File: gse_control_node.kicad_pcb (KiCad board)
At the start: 4 copper layers, 111.5 x 77 mm, 130 parts, among them J1 Conn_01x04, J10 Conn_01x04, J2 Conn_01x02, J3 Conn_02x01, J4 Conn_01x02, J5 Conn_01x02, J6 Conn_01x02, J7 Conn_02x04_Counter_Clockwise, J8 Conn_02x04_Counter_Clockwise, J9 Conn_01x04, Q3 BSS138, Q4 BSS138, Q5 BSS138, U1 ESP32-S2-DevKitC-1, U2 LM3880-1AA, U3 LMR33630BDDA, U4 LMR33630BDDA, U5 TPS78533QKVURQ1, U6 TPS78450QDBVRQ1, U7 ADS112C04, U8 ADS112C04, U9 ADS112C04

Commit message: do some pcb routing
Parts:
- removed C34, C35, C38, C39, C40, C41: 150nF, Capacitor_SMD:C_0402_1005Metric
- removed C36, C37: 0.1μF, Capacitor_SMD:C_0402_1005Metric
- removed D15, D16, D17: BAT54SW, Package_TO_SOT_SMD:SOT-323_SC-70
- removed D18, D19, D20: SK44BL, Diode_SMD:D_SMB
- removed R32, R33, R34: 1k, Resistor_SMD:R_0402_1005Metric
- removed R35: 10k, Resistor_SMD:R_0402_1005Metric
- removed R36, R38, R40: 100, Resistor_SMD:R_0402_1005Metric
- removed R37, R39, R41: 100k, Resistor_SMD:R_0603_1608Metric
- removed U7, U8, U9: ADS112C04, Package_SO:TSSOP-16_4.4x5mm_P0.65mm
- added CR1: USBLC6-2SC6, Package_TO_SOT_SMD:SOT-23-6, F.Cu at (113.4, 91.5)
- added Q1: DMP6023LE-13, Package_TO_SOT_SMD:SOT-223-3_TabPin2, F.Cu at (97.7, 27.9)
- added Q2: BSS138, Package_TO_SOT_SMD:SOT-23-3, F.Cu at (219.3, 83.0)
- added R13: 100k, Resistor_SMD:R_0603_1608Metric, F.Cu at (104.3, 57.1)
- added R14: 23.2k, Resistor_SMD:R_0603_1608Metric, F.Cu at (105.2, 54.8)
- added R15: 100k, Resistor_SMD:R_0603_1608Metric, F.Cu at (84.6, 56.9)
- added SW1: USAKRO UK-B0227-G4.3-B-250, Button_Switch_SMD:SW_Tactile_SPST_NO_Straight_CK_PTS636Sx25SMTRLFS, F.Cu at (139.5, 93.5)
- added SW2: USAKRO UK-B0227-G4.3-B-250, Button_Switch_SMD:SW_Tactile_SPST_NO_Straight_CK_PTS636Sx25SMTRLFS, F.Cu at (139.5, 98.8)
- added TP3: TP_+3.3V, TestPoint:TestPoint_Pad_D1.0mm, F.Cu at (163.0, 27.4)
- added TP4: TP_+5V, TestPoint:TestPoint_Pad_D1.0mm, F.Cu at (163.0, 30.5)
- C1: value 10uF -> 0.1μF; footprint Capacitor_SMD:C_1206_3216Metric -> Capacitor_SMD:C_0402_1005Metric
- C10: value 10uF -> 220nF; footprint Capacitor_SMD:C_1206_3216Metric -> Capacitor_SMD:C_0805_2012Metric
- C11: value 22uF -> 1uF; footprint Capacitor_SMD:C_0805_2012Metric -> Capacitor_SMD:C_0603_1608Metric
- C12: value 220nF -> 1uF; footprint Capacitor_SMD:C_0805_2012Metric -> Capacitor_SMD:C_0603_1608Metric
- C14: value 1uF -> 0.1μF; footprint Capacitor_SMD:C_0603_1608Metric -> Capacitor_SMD:C_0402_1005Metric
- C15: value 0.1μF -> 100uF; footprint Capacitor_SMD:C_0402_1005Metric -> Capacitor_SMD:CP_Elec_10x10
- C16: value 10uF -> 3pF; footprint Capacitor_SMD:C_0805_2012Metric -> Capacitor_SMD:C_0603_1608Metric
- C18: value 22uF -> 10uF; footprint Capacitor_SMD:C_0805_2012Metric -> Capacitor_SMD:C_1812_4532Metric
- C2: value 220nF -> 0.1μF; footprint Capacitor_SMD:C_0805_2012Metric -> Capacitor_SMD:C_0402_1005Metric
- C20, C22: value 10uF -> 22uF
- C21: value 0.1μF -> 22uF; footprint Capacitor_SMD:C_0402_1005Metric -> Capacitor_SMD:C_0805_2012Metric
- C23: value 10uF -> 0.1μF; footprint Capacitor_SMD:C_0805_2012Metric -> Capacitor_SMD:C_0402_1005Metric
- C25: value 0.1μF -> 10uF; footprint Capacitor_SMD:C_0402_1005Metric -> Capacitor_SMD:C_0805_2012Metric
- C26, C27, C28: value 150nF -> 10uF; footprint Capacitor_SMD:C_0402_1005Metric -> Capacitor_SMD:C_0805_2012Metric
- C29: value 150nF -> 22uF; footprint Capacitor_SMD:C_0402_1005Metric -> Capacitor_SMD:C_0805_2012Metric
- C3: value 0.1μF -> 150nF
- C31: value 0.1μF -> 1uF; footprint Capacitor_SMD:C_0402_1005Metric -> Capacitor_SMD:C_0603_1608Metric
- C32, C33: value 150nF -> 0.1μF
- C4: value 1uF -> 150nF; footprint Capacitor_SMD:C_0603_1608Metric -> Capacitor_SMD:C_0402_1005Metric
- C5: value 100uF -> 150nF; footprint Capacitor_SMD:CP_Elec_10x10 -> Capacitor_SMD:C_0402_1005Metric
- C6: value 10uF -> 150nF; footprint Capacitor_SMD:C_1812_4532Metric -> Capacitor_SMD:C_0402_1005Metric
- C7: value 0.1μF -> 10uF; footprint Capacitor_SMD:C_0402_1005Metric -> Capacitor_SMD:C_1206_3216Metric
- C8: value 3pF -> 10uF; footprint Capacitor_SMD:C_0603_1608Metric -> Capacitor_SMD:C_1206_3216Metric
- C9: value 22uF -> 220nF
- D1: value LED-Y -> BAT54SW; footprint LED_SMD:LED_0805_2012Metric -> Package_TO_SOT_SMD:SOT-323_SC-70
- D10: value BAT54SW -> LED-Y; footprint Package_TO_SOT_SMD:SOT-323_SC-70 -> LED_SMD:LED_0805_2012Metric
- D11, D12, D13, D14: value BAT54SW -> SK44BL; footprint Package_TO_SOT_SMD:SOT-323_SC-70 -> Diode_SMD:D_SMB
- D2: value SMCJ26A-13-F -> BAT54SW; footprint Diode_SMD:D_SMC -> Package_TO_SOT_SMD:SOT-323_SC-70
- D3, D4: value LED-G -> BAT54SW; footprint LED_SMD:LED_0805_2012Metric -> Package_TO_SOT_SMD:SOT-323_SC-70
- D5: value LED-G -> SMCJ26A-13-F; footprint LED_SMD:LED_0805_2012Metric -> Diode_SMD:D_SMC
- D6: value BAT54SW -> 12V_Z; footprint Package_TO_SOT_SMD:SOT-323_SC-70 -> Diode_SMD:D_SOD-123
- D7, D8, D9: value BAT54SW -> LED-G; footprint Package_TO_SOT_SMD:SOT-323_SC-70 -> LED_SMD:LED_0805_2012Metric
- J1: value Conn_01x04 -> Screw_Terminal_01x02; footprint Connector_JST:JST_EH_B4B-EH-A_1x04_P2.50mm_Vertical -> TerminalBlock_Phoenix:TerminalBlock_Phoenix_MKDS-1,5-2_1x02_P5.00mm_Horizontal
- J10, J9: value Conn_01x04 -> Conn_01x02; footprint Connector_JST:JST_EH_B4B-EH-A_1x04_P2.50mm_Vertical -> Connector_Molex:Molex_Micro-Fit_3.0_43650-0215_1x02_P3.00mm_Vertical
- J2: value Conn_01x02 -> Conn_01x04; footprint Connector_Molex:Molex_Micro-Fit_3.0_43650-0215_1x02_P3.00mm_Vertical -> Connector_Molex:Molex_KK-254_AE-6410-04A_1x04_P2.54mm_Vertical
- J3: value Conn_02x01 -> 4-Pin Load Cell; footprint Connector_Molex:Molex_Mini-Fit_Jr_5566-02A_2x01_P4.20mm_Vertical -> Connector_Molex:Molex_Micro-Fit_3.0_43650-0415_1x04_P3.00mm_Vertical
- J4: value Conn_01x02 -> Conn_02x01; footprint Connector_JST:JST_EH_B2B-EH-A_1x02_P2.50mm_Vertical -> Connector_Molex:Molex_Mini-Fit_Jr_5566-02A_2x01_P4.20mm_Vertical
- J5: value Conn_01x02 -> USB_C_Receptacle_USB2.0_16P; footprint Connector_JST:JST_EH_B2B-EH-A_1x02_P2.50mm_Vertical -> Connector_USB:USB_C_Receptacle_G-Switch_GT-USB-7051x
- J6: value Conn_01x02 -> Conn_01x04; footprint Connector_JST:JST_EH_B2B-EH-A_1x02_P2.50mm_Vertical -> Connector_Molex:Molex_KK-254_AE-6410-04A_1x04_P2.54mm_Vertical
- J7, J8: value Conn_02x04_Counter_Clockwise -> Conn_01x02; footprint Connector_JST:JST_J2100_B08B-J21DK-GGXR_2x04_P2.50x4.00mm_Vertical -> Connector_Molex:Molex_Micro-Fit_3.0_43650-0215_1x02_P3.00mm_Vertical
- L1: value 16uH -> 4.7uH
- R12: value 9.09k -> 100k
- R16: value 100k -> 9.09k
- R17: value 100k -> 39k; footprint Resistor_SMD:R_0603_1608Metric -> Resistor_SMD:R_0402_1005Metric
- R18: value 23.2k -> 1.2k; footprint Resistor_SMD:R_0603_1608Metric -> Resistor_SMD:R_0402_1005Metric
- R19: value 1.2k -> 3.3k
- R2, R3: value 3.3k -> 1k
- R20: value 3.3k -> 10k
- R22, R23: value 1k -> 5.1k
- R24, R26, R28: value 1k -> 100
- R25: value 10k -> 100k; footprint Resistor_SMD:R_0402_1005Metric -> Resistor_SMD:R_0603_1608Metric
- R27, R29, R31: value 1k -> 100k; footprint Resistor_SMD:R_0402_1005Metric -> Resistor_SMD:R_0603_1608Metric
- R30: value 10k -> 100
- R5, R6, R7: value 100k -> 1k; footprint Resistor_SMD:R_0603_1608Metric -> Resistor_SMD:R_0402_1005Metric
- R8: value 39k -> 10k
- R9: value 100k -> 10k
- TP1: value TP_+3.3V -> SDA; footprint TestPoint:TestPoint_Pad_D1.0mm -> TestPoint:TestPoint_Pad_D1.5mm
- TP2: value TP_+5V -> SCL; footprint TestPoint:TestPoint_Pad_D1.0mm -> TestPoint:TestPoint_Pad_D1.5mm
- U1: value ESP32-S2-DevKitC-1 -> ADS112C04; footprint PCM_Espressif:ESP32-S2-DevKitC-1 -> Package_SO:TSSOP-16_4.4x5mm_P0.65mm
- U2: value LM3880-1AA -> LMR33630BDDA; footprint Package_TO_SOT_SMD:SOT-23-6 -> Package_SO:Texas_HSOP-8-1EP_3.9x4.9mm_P1.27mm_ThermalVias
- U4: value LMR33630BDDA -> TPS78533QKVURQ1; footprint Package_SO:Texas_HSOP-8-1EP_3.9x4.9mm_P1.27mm_ThermalVias -> Package_TO_SOT_SMD:TO-252-4
- U5: value TPS78533QKVURQ1 -> TPS78450QDBVRQ1; footprint Package_TO_SOT_SMD:TO-252-4 -> Package_TO_SOT_SMD:SOT-23-5
- U6: value TPS78450QDBVRQ1 -> ESP32-S3-WROOM-1U; footprint Package_TO_SOT_SMD:SOT-23-5 -> RF_Module:ESP32-S3-WROOM-1U
- moved H2 205.6 mm to (22.4, 175.2)
- moved H4 181.4 mm to (22.4, 189.7)
- moved J10 138.7 mm to (229.7, 110.0)
- moved J9 138.4 mm to (229.7, 101.3)
- moved H1 129.4 mm to (22.4, 167.9)
- moved J2 118.7 mm to (41.8, 94.0), turned to 0 degrees
- moved Q4 117.9 mm to (219.3, 100.2)
- moved Q5 114.9 mm to (219.3, 108.8)
- moved Q3 107.8 mm to (219.3, 91.6)
- moved D1 103.5 mm to (131.9, 164.2), turned to 0 degrees
- moved C24 103.0 mm to (74.9, 47.9), turned to 90 degrees
- moved R3 102.7 mm to (120.3, 156.8), turned to 0 degrees
- moved C20 102.1 mm to (71.1, 47.5)
- moved D6 101.9 mm to (97.7, 34.9)
- moved D5 95.9 mm to (88.4, 27.8), turned to 90 degrees
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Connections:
- C1 pad 1: +24V -> +3.3V
- C11 pad 1: +12V -> /Power Regulation/VCC_5.3
- C12 pad 1: +24V -> /Power Regulation/VCC_12
- C13 pad 1: GND -> Net-(U2-BOOT)
- C13 pad 2: +12V -> /Power Regulation/SW_5.3
- C14 pad 1: /Power_Regulation/VCC-5 -> Net-(U3-BOOT)
- C14 pad 2: GND -> /Power Regulation/SW_12
- C15 pad 1: Net-(U4-BOOT) -> +24V
- C15 pad 2: /Power_Regulation/SW-5 -> GND
- C16 pad 1: /Power_Regulation/+5.3V -> /Power Regulation/+5.3V
- C16 pad 2: GND -> Net-(U2-FB)
- C17 pad 1: /Power_Regulation/+5.3V -> +12V
- C17 pad 2: Net-(U4-FB) -> Net-(U3-FB)
- C18 pad 1: /Power_Regulation/+5.3V -> +24V
- C19 pad 1: /Power_Regulation/+5.3V -> /Power Regulation/+5.3V
- C2 pad 1: +24V -> +5V
- C20 pad 1: +3.3V -> +12V
- C21 pad 1: GND -> /Power Regulation/+5.3V
- C21 pad 2: /Power_Regulation/+5.3V -> GND
- C22 pad 1: /Power_Regulation/+5.3V -> +12V
- C23 pad 1: +5V -> GND
- C23 pad 2: GND -> /Power Regulation/+5.3V
- C24 pad 1: +3.3V -> GND
- C24 pad 2: GND -> +12V
- C25 pad 1: +5V -> /Power Regulation/+5.3V
- C26 pad 1: /ADC1/AIN3 -> +3.3V
- C27 pad 1: /ADC1/AIN0 -> /Power Regulation/+5.3V
- C28 pad 1: /ADC1/AIN2 -> +5V
- C29 pad 1: /ADC1/AIN1 -> +3.3V
- C3 pad 1: GND -> /ADC 1/AIN3
- C3 pad 2: /Power_Regulation/+5.3V -> GND
- C31 pad 1: +5V -> /ESP32 Breakout/RESET
- C32 pad 1: /ADC2/AIN3 -> /ESP32 Breakout/RESET
- C33 pad 1: /ADC2/AIN0 -> 5V_USB
- C4 pad 1: /Power_Regulation/VCC-12 -> /ADC 1/AIN0
- C5 pad 1: +24V -> /ADC 1/AIN2
- C6 pad 1: +24V -> /ADC 1/AIN1
- C7 pad 1: Net-(U3-BOOT) -> +24V
- C7 pad 2: /Power_Regulation/SW-12 -> GND
- C8 pad 1: +12V -> +24V
- C8 pad 2: Net-(U3-FB) -> GND
- C9 pad 1: +12V -> +24V
- D1 pad 2: Net-(D1-A) -> +5V
- D10 pad 2: +5V -> Net-(D10-A)
- D11 pad 1: GND -> +24V
- D11 pad 2: +5V -> Net-(D11-A)
- D12 pad 1: GND -> +24V
- D12 pad 2: +5V -> Net-(D12-A)
- D13 pad 1: GND -> +24V
- D13 pad 2: +5V -> Net-(D13-A)
- D14 pad 1: GND -> +24V
- D14 pad 2: +5V -> Net-(D14-A)
- D2 pad 1: +24V -> GND
- D2 pad 2: GND -> +5V
- D3 pad 2: Net-(D3-A) -> +5V
- D4 pad 2: Net-(D4-A) -> +5V
- D5 pad 1: GND -> Net-(D5-A1)
- D5 pad 2: Net-(D5-A) -> GND
- D6 pad 1: GND -> +24V
- D6 pad 2: +5V -> Net-(D6-A)
- D7 pad 2: +5V -> Net-(D7-A)
- D8 pad 2: +5V -> Net-(D8-A)
- D9 pad 2: +5V -> Net-(D9-A)
- F1 pad 1: Net-(J3-Pin_1) -> Net-(J4-Pin_1)
- F1 pad 2: +24V -> Net-(D5-A1)
- J1 pad 1: +5V -> /ADC 1/SIG0
- J1 pad 2: Load_Cell+ -> /ADC 1/SIG1
- J10 pad 1: GND -> +24V
- J10 pad 2: +12V -> Net-(D14-A)
- J2 pad 1: Net-(J2-Pin_1) -> GND
- J2 pad 2: /Power_Regulation/+5.3V -> +12V
- J3 pad 1: Net-(J3-Pin_1) -> +5V
- J3 pad 2: GND -> LOAD_CELL+
- J4 pad 1: +24V -> Net-(J4-Pin_1)
- J4 pad 2: Net-(D18-A) -> GND
- J6 pad 1: +24V -> GND
- J6 pad 2: Net-(D20-A) -> +12V
- J7 pad 1: +3.3V -> +24V
- J7 pad 2: Heat_1_Variable -> Net-(D11-A)
- J8 pad 1: +3.3V -> +24V
- J8 pad 2: Heat_2_Variable -> Net-(D12-A)
- J9 pad 1: GND -> +24V
- J9 pad 2: +12V -> Net-(D13-A)
- L1 pad 1: /Power_Regulation/SW-12 -> /Power Regulation/SW_5.3
- L1 pad 2: +12V -> /Power Regulation/+5.3V
- L2 pad 1: /Power_Regulation/SW-5 -> /Power Regulation/SW_12
- L2 pad 2: /Power_Regulation/+5.3V -> +12V
- Q3 pad 3: Net-(D18-A) -> Net-(D12-A)
- Q4 pad 3: Net-(D19-A) -> Net-(D13-A)
- Q5 pad 3: Net-(D20-A) -> Net-(D14-A)
- R10 pad 1: /Power_Regulation/+12_EN -> /Power Regulation/5.3_POWER_GOOD
- R10 pad 2: /Power_Regulation/+5.3V -> +3.3V
- R11 pad 1: +12V -> 12V_GOOD
- R11 pad 2: Net-(U3-FB) -> +3.3V
- R12 pad 1: Net-(U3-FB) -> +24V
- R12 pad 2: GND -> Net-(D6-A)
- R16 pad 1: 24V_GOOD -> Net-(U3-FB)
- R16 pad 2: +3.3V -> GND
- R17 pad 1: /Power_Regulation/+5.3V -> Net-(D7-A)
- R17 pad 2: Net-(U4-FB) -> +24V
- R18 pad 1: Net-(U4-FB) -> Net-(D8-A)
- R18 pad 2: GND -> +3.3V
- R19 pad 1: Net-(D4-A) -> Net-(D9-A)
- R19 pad 2: +3.3V -> +5V
- R2 pad 1: +3.3V -> I2C_SCL
- R2 pad 2: DRDY3 -> +3.3V
- R20 pad 1: Net-(D5-A) -> /ESP32 Breakout/RESET
- R20 pad 2: +5V -> +3.3V
- R21 pad 1: Heat_2_Current -> Net-(D10-A)
- R21 pad 2: /ADC1/AIN3 -> /ESP32 Breakout/WIFI_IND
- R22 pad 1: Load_Cell+ -> Net-(J5-CC1)
- R22 pad 2: /ADC1/AIN2 -> GND
- R23 pad 1: Load_Cell- -> Net-(J5-CC2)
- R23 pad 2: /ADC1/AIN1 -> GND
- R24 pad 1: Heat_1_Current -> ACTUATOR_1_CTL
- R24 pad 2: /ADC1/AIN0 -> Net-(Q2-G)
- R25 pad 1: +3.3V -> Net-(Q2-G)
- R25 pad 2: Net-(U7-RESET) -> GND
- R26 pad 1: Heat_1_TC -> ACTUATOR_2_CTL
- R26 pad 2: /ADC2/AIN3 -> Net-(Q3-G)
- R27 pad 1: Heat_1_TB -> Net-(Q3-G)
- R27 pad 2: /ADC2/AIN2 -> GND
- R28 pad 1: Heat_1_TA -> ACTUATOR_3_CTL
- R28 pad 2: /ADC2/AIN1 -> Net-(Q4-G)
- R29 pad 1: Heat_1_Variable -> Net-(Q4-G)
- R29 pad 2: /ADC2/AIN0 -> GND
- R3 pad 1: +3.3V -> I2C_SDA
- R3 pad 2: DRDY2 -> +3.3V
- R30 pad 1: +3.3V -> ACTUATOR_4_CTL
- R30 pad 2: Net-(U8-RESET) -> Net-(Q5-G)
- R31 pad 1: Heat_2_TC -> Net-(Q5-G)
- R31 pad 2: /ADC3/AIN3 -> GND
- R4 pad 1: Net-(D1-A) -> LOAD_CELL+
- R4 pad 2: /ESP32-Breakout/WIFI_IND -> /ADC 1/AIN3
- R5 pad 1: GND -> LOAD_CELL-
- R5 pad 2: Net-(J2-Pin_1) -> /ADC 1/AIN2
- R6 pad 1: /Power_Regulation/+3.3V_EN -> /ADC 1/SIG1
- R6 pad 2: /Power_Regulation/+5.3V -> /ADC 1/AIN1
- R7 pad 1: /Power_Regulation/+5V_EN -> /ADC 1/SIG0
- R7 pad 2: /Power_Regulation/+5.3V -> /ADC 1/AIN0
- R8 pad 1: Net-(D3-A) -> +3.3V
- R8 pad 2: +24V -> Net-(U1-RESET)
- R9 pad 1: 12V_GOOD -> Net-(D6-A)
- R9 pad 2: +3.3V -> GND
- TP1 pad 1: +3.3V -> I2C_SCL
- TP2 pad 1: +5V -> I2C_SDA
- U1 pad 1: unconnected-(U1-3V3-Pad1) -> GND
- U1 pad 10: unconnected-(U1-GPIO17/ADC2_CH6/U1TXD-Pad10) -> /ADC 1/AIN1
- U1 pad 11: unconnected-(U1-GPIO18/ADC2_CH7/U1RXD-Pad11) -> /ADC 1/AIN0
- U1 pad 12: Fan_2_Control -> +5V
- U1 pad 13: Fan_2_PWM -> +3.3V
- U1 pad 14: Nitrous_Control -> DRDY1
- U1 pad 15: 24V_GOOD -> I2C_SDA
- U1 pad 16: 12V_GOOD -> I2C_SCL
- U1 pad 2: unconnected-(U1-3V3-Pad2) -> GND
- U1 pad 3: unconnected-(U1-RST-Pad3) -> Net-(U1-RESET)
- U1 pad 4: A1_Control -> GND
- U1 pad 5: A2_Control -> GND
- U1 pad 6: Fan_1_Control -> /ADC 1/AIN3
- U1 pad 7: Fan_1_PWM -> /ADC 1/AIN2
- U2 pad 1: /Power_Regulation/+5.3V -> GND
- U2 pad 2: GND -> +24V
- U2 pad 3: Net-(J2-Pin_1) -> +24V
- U2 pad 4: /Power_Regulation/+12_EN -> /Power Regulation/5.3_POWER_GOOD
- U2 pad 5: /Power_Regulation/+5V_EN -> Net-(U2-FB)
- U2 pad 6: /Power_Regulation/+3.3V_EN -> /Power Regulation/VCC_5.3
- U3 pad 3: /Power_Regulation/+12_EN -> +24V
- U3 pad 6: /Power_Regulation/VCC-12 -> /Power Regulation/VCC_12
- U3 pad 8: /Power_Regulation/SW-12 -> /Power Regulation/SW_12
- U4 pad 1: GND -> /Power Regulation/+5.3V
- U4 pad 2: +24V -> /Power Regulation/+5.3V
- U4 pad 3: +24V -> GND
- U4 pad 4: 24V_GOOD -> +3.3V
- U4 pad 5: Net-(U4-FB) -> (no net)
- U5 pad 1: /Power_Regulation/+3.3V_EN -> /Power Regulation/+5.3V
- U5 pad 2: /Power_Regulation/+5.3V -> GND
- U5 pad 3: GND -> /Power Regulation/+5.3V
- U5 pad 4: +3.3V -> GND
- U5 pad 5: (no net) -> +5V
- U6 pad 1: /Power_Regulation/+5.3V -> GND
- U6 pad 2: GND -> +3.3V
- U6 pad 3: /Power_Regulation/+5V_EN -> /ESP32 Breakout/RESET
- U6 pad 4: GND -> unconnected-(U6-IO4-Pad4)
- U6 pad 5: +5V -> unconnected-(U6-IO5-Pad5)
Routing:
- net +3.3V: track 204.8 -> 7.61 mm, vias 20 -> 0
- net GND: track 139.3 -> 4.81 mm, vias 120 -> 0
- net /Power_Regulation/+5.3V: track 132.8 -> 0.00 mm, vias 6 -> 0
- net +24V: track 154.0 -> 29.0 mm, vias 9 -> 4
- net +5V: track 126.2 -> 2.15 mm, vias 18 -> 0
- net I2C_Clock: track 62.4 -> 0.00 mm, vias 2 -> 0
- net I2C_Data: track 56.7 -> 0.00 mm
- net /Power_Regulation/+12_EN: track 54.5 -> 0.00 mm, vias 2 -> 0
- net /Power_Regulation/+5V_EN: track 46.7 -> 0.00 mm, vias 2 -> 0
- net /Power_Regulation/+3.3V_EN: track 39.6 -> 0.00 mm, vias 2 -> 0
- net /Power Regulation/+5.3V: track 0.00 -> 35.4 mm, vias 0 -> 3
- net Fan_2_Control: track 33.7 -> 0.00 mm, vias 2 -> 0
- net Fan_1_Control: track 31.7 -> 0.00 mm, vias 2 -> 0
- net Fan_2_PWM: track 31.2 -> 0.00 mm, vias 2 -> 0
- net DRDY1: track 30.4 -> 0.00 mm, vias 2 -> 0
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- added copper zone on F.Cu, net +12V
- added copper zone on F.Cu, net +24V
- added copper zone on F.Cu, net /Power Regulation/+5.3V
- added copper zone on F.Cu, net /Power Regulation/SW_12
- added copper zone on F.Cu, net /Power Regulation/SW_5.3
- added copper zone on F.Cu, net GND
- added copper zone on F.Cu, net Net-(U2-FB)
- added copper zone on F.Cu, net Net-(U3-FB)
- removed copper zone on In1.Cu, net GND
- removed copper zone on In2.Cu, net GND
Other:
- board outline removed
- board text removed: "12V Step-Down"
- board text removed: "24V Input"
- board text removed: "24V ON"
- board text removed: "3.3V Regulation"
- board text removed: "5.3V Step-Down"
- board text removed: "5V Regulation"
- board text removed: "Actuator 1"
- board text removed: "Actuator 2"
- board text removed: "Fans 1&2"
- board text removed: "Ground Support Equipment PCB Draft 2 2026-04-07"
- board text removed: "Heating Control System 1"
- board text removed: "Heating Control System 2"
- board text removed: "Load Cell"
- board text removed: "Nitrous Actuator"
- board text removed: "Notes pre-review: Is there a better place to put Power Sequencing? This one puts it close to 3.3V and 5V, but not 12V. Is there a better way to place things to avoid snaking lines over/under eachother? Are the sockets too close to eachother to be practically soldered/used? Should I be worried about capacitance of the 2 inner plates in the zones devoid of GND vias?"
- board text removed: "Power Sequencing"
- board text removed: "WIFI ON"

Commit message: finish pcb routing
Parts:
- removed TP1: SDA, TestPoint:TestPoint_Pad_D1.5mm
- removed TP2: SCL, TestPoint:TestPoint_Pad_D1.5mm
- added C34: 0.1μF, Capacitor_SMD:C_0402_1005Metric, F.Cu at (134.1, 95.8)
- added C35: 0.1μF, Capacitor_SMD:C_0402_1005Metric, F.Cu at (138.4, 97.2)
- added C36: 0.1μF, Capacitor_SMD:C_0402_1005Metric, F.Cu at (138.0, 95.7)
- added TP5: GND_TP, TestPoint:TestPoint_Loop_D2.50mm_Drill1.0mm, F.Cu at (168.0, 66.7)
- added TP6: 24V_TP, TestPoint:TestPoint_Loop_D2.50mm_Drill1.0mm, F.Cu at (163.5, 66.7)
- added U7: LM66200DRLR, Package_TO_SOT_SMD:SOT-583-8, F.Cu at (136.1, 96.2)
- R14: value 23.2k -> 24k
- moved H2 186.8 mm to (174.5, 66.7)
- moved H4 166.6 mm to (174.5, 121.7)
- moved H1 140.2 mm to (119.5, 66.7)
- moved H3 114.5 mm to (119.5, 121.7)
- moved TP3 77.6 mm to (158.9, 104.9), turned to 180 degrees
- moved J2 76.5 mm to (118.2, 96.2), turned to -90 degrees
- moved TP4 74.4 mm to (163.1, 104.9)
- moved C19 71.8 mm to (148.4, 90.5), turned to 0 degrees
- moved C8 70.5 mm to (152.6, 88.8), turned to 180 degrees
- moved C21 68.8 mm to (148.4, 88.4), turned to 0 degrees
- moved R10 68.4 mm to (156.2, 86.2), turned to 0 degrees
- moved D5 68.0 mm to (136.3, 76.1), turned to 0 degrees
- moved C10 67.2 mm to (152.0, 86.5), turned to 180 degrees
- moved J1 67.1 mm to (173.7, 112.9), turned to 90 degrees
- moved C23 66.5 mm to (148.8, 86.7), turned to 180 degrees
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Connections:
- C16 pad 1: /Power Regulation/+5.3V -> /Power Regulation/+5.17V_PRE
- C19 pad 1: /Power Regulation/+5.3V -> /Power Regulation/+5.17V_PRE
- C21 pad 1: /Power Regulation/+5.3V -> /Power Regulation/+5.17V_PRE
- C23 pad 2: /Power Regulation/+5.3V -> /Power Regulation/+5.17V_PRE
- C25 pad 1: /Power Regulation/+5.3V -> /Power Regulation/+5.17V
- C27 pad 1: /Power Regulation/+5.3V -> /Power Regulation/+5.17V
- J5 pad SH: (no net) -> GND
- L1 pad 2: /Power Regulation/+5.3V -> /Power Regulation/+5.17V_PRE
- R10 pad 1: /Power Regulation/5.3_POWER_GOOD -> 5.17V_PG
- R11 pad 1: 12V_GOOD -> 12V_PG
- R13 pad 1: /Power Regulation/+5.3V -> /Power Regulation/+5.17V_PRE
- U2 pad 4: /Power Regulation/5.3_POWER_GOOD -> 5.17V_PG
- U3 pad 4: 12V_GOOD -> 12V_PG
- U4 pad 1: /Power Regulation/+5.3V -> /Power Regulation/+5.17V
- U4 pad 2: /Power Regulation/+5.3V -> /Power Regulation/+5.17V
- U5 pad 1: /Power Regulation/+5.3V -> /Power Regulation/+5.17V
- U5 pad 3: /Power Regulation/+5.3V -> /Power Regulation/+5.17V
- U6 pad 10: unconnected-(U6-IO17-Pad10) -> ACTUATOR_2_CTL
- U6 pad 12: unconnected-(U6-IO8-Pad12) -> ACTUATOR_1_CTL
- U6 pad 22: unconnected-(U6-IO14-Pad22) -> 5.17V_PG
- U6 pad 23: unconnected-(U6-IO21-Pad23) -> 12V_PG
- U6 pad 32: unconnected-(U6-IO39-Pad32) -> FAN_1_TACH
- U6 pad 33: unconnected-(U6-IO40-Pad33) -> FAN_1_PWM
- U6 pad 34: unconnected-(U6-IO41-Pad34) -> FAN_2_TACH
- U6 pad 35: unconnected-(U6-IO42-Pad35) -> FAN_2_PWM
- U6 pad 5: unconnected-(U6-IO5-Pad5) -> DRDY1
- U6 pad 6: unconnected-(U6-IO6-Pad6) -> I2C_SDA
- U6 pad 7: unconnected-(U6-IO7-Pad7) -> I2C_SCL
- U6 pad 8: unconnected-(U6-IO15-Pad8) -> ACTUATOR_4_CTL
- U6 pad 9: unconnected-(U6-IO16-Pad9) -> ACTUATOR_3_CTL
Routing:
- net GND: track 4.81 -> 81.2 mm, vias 0 -> 68
- net +24V: track 29.0 -> 92.6 mm, vias 4 -> 7
- net +5V: track 2.15 -> 63.0 mm, vias 0 -> 6
- net ACTUATOR_1_CTL: track 0.00 -> 46.6 mm
- net 5V_USB: track 0.00 -> 46.1 mm, vias 0 -> 2
- net /Power Regulation/+5.17V_PRE: track 0.00 -> 45.4 mm, vias 0 -> 5
- net 5.17V_PG: track 0.00 -> 41.2 mm, vias 0 -> 2
- net ACTUATOR_2_CTL: track 0.00 -> 38.5 mm
- net /Power Regulation/+5.3V: track 35.4 -> 0.00 mm, vias 3 -> 0
- net ACTUATOR_3_CTL: track 0.00 -> 32.3 mm
- net +3.3V: track 7.61 -> 37.4 mm, vias 0 -> 9
- net /ESP32 Breakout/RESET: track 3.68 -> 31.9 mm, vias 0 -> 2
- net ACTUATOR_4_CTL: track 0.00 -> 24.5 mm
- net /Power Regulation/+5.17V: track 0.00 -> 23.5 mm
- net +12V: track 26.1 -> 2.60 mm
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- added copper zone on B.Cu, net +12V
- added copper zone on B.Cu, net +24V
- added copper zone on B.Cu, net +3.3V
- added copper zone on F.Cu, net /Power Regulation/+5.17V_PRE
- added copper zone on In1.Cu, net GND
- added copper zone on In2.Cu, net GND
- removed copper zone on F.Cu, net /Power Regulation/+5.3V
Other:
- board outline added: 65 x 65 mm
- board text added: "24V"
- board text added: "24V_IN"
- board text added: "24V_TP"
- board text added: "3.3V"
- board text added: "3.3V_TP"
- board text added: "5V"
- board text added: "5V_TP"
- board text added: "ACT1"
- board text added: "ACT2"
- board text added: "ACT3"
- board text added: "ACT4"
- board text added: "BOOT"
- board text added: "FAN1"
- board text added: "FAN2"
- board text added: "GND_TP"
- board text added: "LOAD_CELL"
- board text added: "RESET"
- board text added: "SIG0"
- board text added: "SIG1"
- board text added: "WIFI_IND"

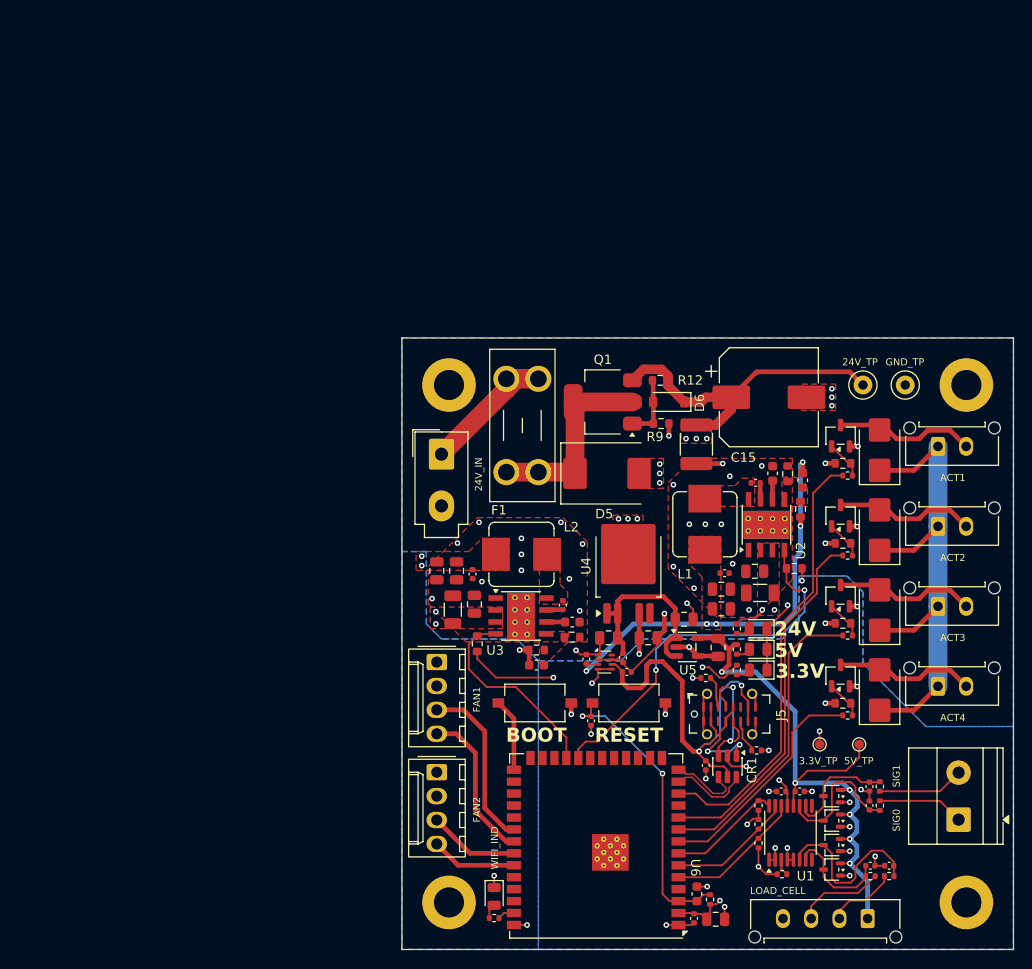
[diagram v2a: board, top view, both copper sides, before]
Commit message: remove unneccesary component fields
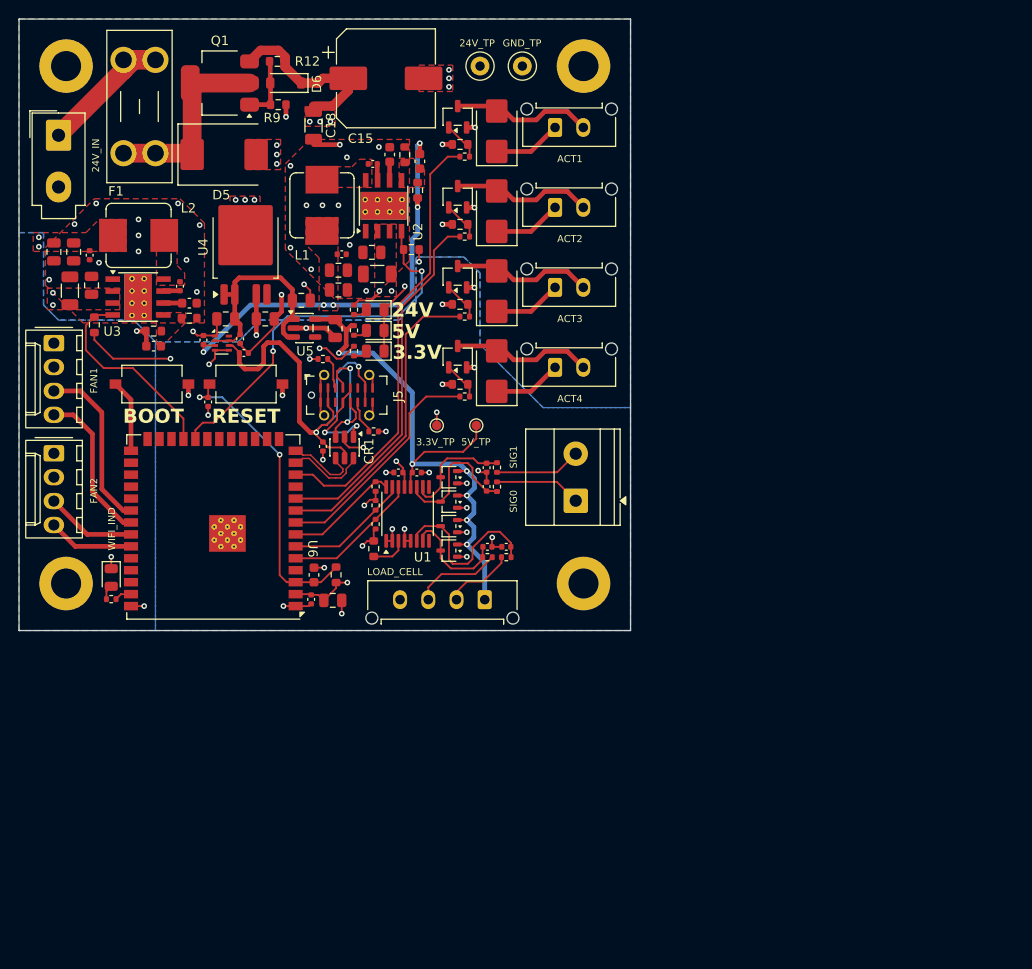
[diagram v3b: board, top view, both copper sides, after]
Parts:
- C1, C13, C14, C2, C23, C24, C30, C32, C33, C34, C35, C36: value 0.1μF -> 100nF
- C18: footprint Capacitor_SMD:C_1812_4532Metric -> Capacitor_SMD:C_1206_3216Metric
- J3: value 4-Pin Load Cell -> Conn_01x04
- R1, R19: value 3.3k -> 3.3kΩ
- R10, R11, R12, R13, R15, R25, R27, R29, R31: value 100k -> 100kΩ
- R14: value 24k -> 24kΩ
- R16: value 9.09k -> 9.09kΩ
- R17: value 39k -> 39kΩ
- R18: value 1.2k -> 1.2kΩ
- R2, R21, R3, R4, R5, R6, R7: value 1k -> 1kΩ
- R20, R8: value 10k -> 10kΩ; footprint Resistor_SMD:R_0402_1005Metric -> Resistor_SMD:R_0603_1608Metric
- R22, R23: value 5.1k -> 5.1kΩ
- R24, R26, R28, R30: value 100 -> 100Ω
- R9: value 10k -> 10kΩ
- U7: value LM66200DRLR -> LM66200
- moved R8 55.5 mm to (111.5, 84.1), turned to -90 degrees
- moved C12 53.0 mm to (91.9, 58.0)
- moved C23 53.0 mm to (108.1, 52.8)
- moved C26 53.0 mm to (100.0, 59.7)
- moved C30 53.0 mm to (104.8, 89.5)
- moved C33 53.0 mm to (106.1, 73.2)
- moved J1 53.0 mm to (133.0, 79.0)
- moved J5 53.0 mm to (108.6, 67.8)
- moved R6 53.0 mm to (124.6, 75.5)
- moved C18 53.0 mm to (105.1, 39.1)
- moved D8 53.0 mm to (111.7, 63.1)
- moved D9 53.0 mm to (111.7, 60.9)
- moved R22 53.0 mm to (106.1, 63.9)
- moved R9 53.0 mm to (101.3, 36.9)
- moved C10 53.0 mm to (111.3, 52.6)
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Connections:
- U4 pad 5: (no net) -> unconnected-(U4-NC-Pad5)
- U5 pad 4: GND -> unconnected-(U5-NC-Pad4)
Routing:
- net +24V: track 92.6 -> 51.4 mm
- net Net-(U1-RESET): track 1.78 -> 3.91 mm
- net /ESP32 Breakout/RESET: track 31.9 -> 33.3 mm
- net +3.3V: track 37.4 -> 36.6 mm

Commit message: add all lcsc part numbers
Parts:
- C3, C4, C5, C6: value 150nF -> 220nF
- R4, R5, R6, R7: value 1kΩ -> 680
